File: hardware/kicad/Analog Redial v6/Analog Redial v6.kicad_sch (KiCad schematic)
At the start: 75 parts, among them J1 Barrel_Jack_PTH_Slot, J2 PINHD_1x8_Male, J3 PINHD_1x2_Male, J4 PINHD_1x2_Male, J5 PINHD_2x4_Male, J7 PINHD_1x3_Male, J8 RJ12, J9 RJ12, U1 ESP32-C6-DevKitC-1, U2 ES8388, U3 AG1171, U4 AG1171, U5 XC6206P332MR

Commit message: v6 board: layout and schematic updates, PCBWay production files (Oct 5)
Co-Authored-By: Claude Sonnet 5.5 <noreply@anthropic.com>
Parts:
- C10, C11, C16, C17, D12, H1, H2, H3, H4, J1, J2, J3, J4, J5, J7, J8, J9, U1, U3, U4: now left out of the parts list
- U5: value XC6206P332MR -> XC6206P362MR
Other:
- note added: "Changes for SMD5 - SMD6: need to move passives in ag1171 footprint area for ag1171 real module... touches caps. bigger esp32 holes! they're a little tight 3.6V or 3.7V regulator for bluetooth module (need to check if we should use it for audio chip also?) Do we want to do SMT 470uF caps?"
- note removed: "Changes for SMD6: need to move passives in ag1171 footprint area for ag1171 real module... touches caps. bigger esp32 holes!"
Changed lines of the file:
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@@
 		)
 	)
-	(text "Changes for SMD6:\nneed to move passives in ag1171 footprint area for ag1171 real module...  touches caps.\n\nbigger esp32 holes!\n\n\n"
+	(text "Changes for SMD5 - SMD6:\nneed to move passives in ag1171 footprint area for ag1171 real module...  touches caps.\nbigger esp32 holes!  they're a little tight\n3.6V or 3.7V regulator for bluetooth module (need to check if we should use it for audio chip also?)\nDo we want to do SMT 470uF caps?\n\n\n\n"
 		(exclude_from_sim no)
 		(at 198.628 61.214 0)
@@
 		(body_style 1)
 		(exclude_from_sim no)
-		(in_bom yes)
+		(in_bom no)
 		(on_board yes)
 		(in_pos_files yes)
@@
 		(body_style 1)
 		(exclude_from_sim no)
-		(in_bom yes)
+		(in_bom no)
 		(on_board yes)
 		(in_pos_files yes)
@@
 		(body_style 1)
 		(exclude_from_sim no)
-		(in_bom yes)
+		(in_bom no)
 		(on_board yes)
 		(in_pos_files yes)
@@
 			)
 		)
-		(property "Value" "XC6206P332MR"
+		(property "Value" "XC6206P362MR"
 			(at 101.6 50.8 0)
 			(show_name no)
@@
 		(body_style 1)
 		(exclude_from_sim no)
-		(in_bom yes)
+		(in_bom no)
 		(on_board yes)
 		(in_pos_files yes)
@@
 		(body_style 1)
 		(exclude_from_sim no)
-		(in_bom yes)
+		(in_bom no)
 		(on_board yes)
 		(in_pos_files yes)
@@
 		(body_style 1)
 		(exclude_from_sim no)
-		(in_bom yes)
+		(in_bom no)
 		(on_board yes)
 		(in_pos_files yes)
@@
 		(body_style 1)
 		(exclude_from_sim no)
-		(in_bom yes)
+		(in_bom no)
 		(on_board yes)
 		(in_pos_files yes)
@@
 		(body_style 1)
 		(exclude_from_sim no)
-		(in_bom yes)
+		(in_bom no)
 		(on_board yes)
 		(in_pos_files yes)
@@
 		(body_style 1)
 		(exclude_from_sim no)
-		(in_bom yes)
+		(in_bom no)
 		(on_board yes)
 		(in_pos_files yes)
@@
 		(body_style 1)
 		(exclude_from_sim no)
-		(in_bom yes)
+		(in_bom no)
 		(on_board yes)
 		(in_pos_files yes)
@@
 		(body_style 1)
 		(exclude_from_sim no)
-		(in_bom yes)
+		(in_bom no)
 		(on_board yes)
 		(in_pos_files yes)
@@
 		(body_style 1)
 		(exclude_from_sim no)
-		(in_bom yes)
+		(in_bom no)
 		(on_board yes)
 		(in_pos_files yes)
@@
 		(body_style 1)
 		(exclude_from_sim no)
-		(in_bom yes)
+		(in_bom no)
 		(on_board yes)
 		(in_pos_files yes)
@@
 		(body_style 1)
 		(exclude_from_sim no)
-		(in_bom yes)
+		(in_bom no)
 		(on_board yes)
 		(in_pos_files yes)
@@
 		(body_style 1)
 		(exclude_from_sim no)
-		(in_bom yes)
+		(in_bom no)
 		(on_board yes)
 		(in_pos_files yes)
@@
 		(body_style 1)
 		(exclude_from_sim no)
-		(in_bom yes)
+		(in_bom no)
 		(on_board yes)
 		(in_pos_files yes)
@@
 		(body_style 1)
 		(exclude_from_sim no)
-		(in_bom yes)
+		(in_bom no)
 		(on_board yes)
 		(in_pos_files yes)
@@
 		(body_style 1)
 		(exclude_from_sim no)
-		(in_bom yes)
+		(in_bom no)
 		(on_board yes)
 		(in_pos_files yes)
@@
 		(body_style 1)
 		(exclude_from_sim no)
-		(in_bom yes)
+		(in_bom no)
 		(on_board yes)
 		(in_pos_files yes)
@@
 		(body_style 1)
 		(exclude_from_sim no)
-		(in_bom yes)
+		(in_bom no)
 		(on_board yes)
 		(in_pos_files yes)

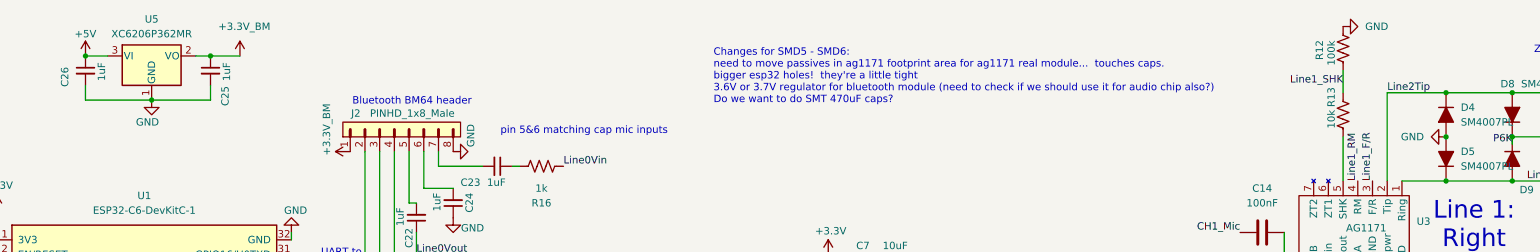
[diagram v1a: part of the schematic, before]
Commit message: v6 board released (untested): clone 5V pin fix, silkscreen updates; JLCPCB export files; docs say untested but should work
U5 stays the 3.3 V XC6206P332MR (JLC Basic); the 3.6 V part was not done.

Co-Authored-By: Claude Sonnet 5.5 <noreply@anthropic.com>
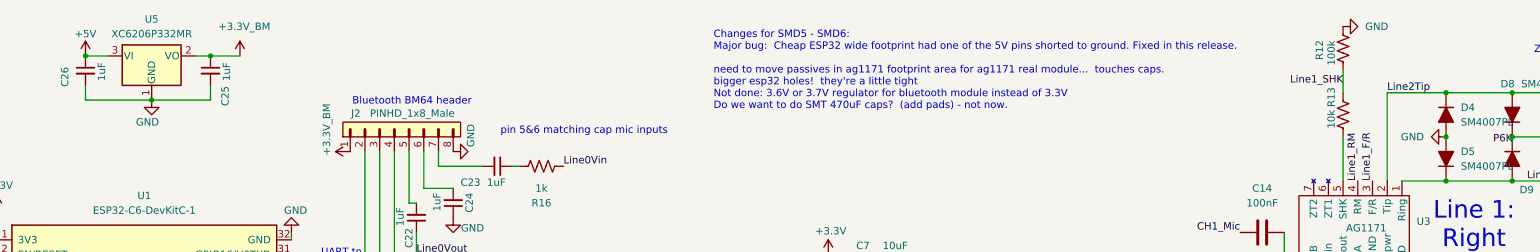
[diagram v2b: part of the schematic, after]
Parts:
- U5: value XC6206P362MR -> XC6206P332MR
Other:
- note added: "Changes for SMD5 - SMD6: Major bug: Cheap ESP32 wide footprint had one of the 5V pins shorted to ground. Fixed in this release. need to move passives in ag1171 footprint area for ag1171 real module... touches caps. bigger esp32 holes! they're a little tight Not done: 3.6V or 3.7V regulator for bluetooth module instead of 3.3V Do we want to do SMT 470uF caps? (add pads) - not now."
- note removed: "Changes for SMD5 - SMD6: need to move passives in ag1171 footprint area for ag1171 real module... touches caps. bigger esp32 holes! they're a little tight 3.6V or 3.7V regulator for bluetooth module (need to check if we should use it for audio chip also?) Do we want to do SMT 470uF caps?"
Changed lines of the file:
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@@
 		)
 	)
-	(text "Changes for SMD5 - SMD6:\nneed to move passives in ag1171 footprint area for ag1171 real module...  touches caps.\nbigger esp32 holes!  they're a little tight\n3.6V or 3.7V regulator for bluetooth module (need to check if we should use it for audio chip also?)\nDo we want to do SMT 470uF caps?\n\n\n\n"
+	(text "Changes for SMD5 - SMD6:\nMajor bug:  Cheap ESP32 wide footprint had one of the 5V pins shorted to ground. Fixed in this release.\n\nneed to move passives in ag1171 footprint area for ag1171 real module...  touches caps.\nbigger esp32 holes!  they're a little tight\nNot done: 3.6V or 3.7V regulator for bluetooth module instead of 3.3V\nDo we want to do SMT 470uF caps?  (add pads) - not now.\n\n\n\n\n"
 		(exclude_from_sim no)
 		(at 198.628 61.214 0)
@@
 			)
 		)
-		(property "Value" "XC6206P362MR"
+		(property "Value" "XC6206P332MR"
 			(at 101.6 50.8 0)
 			(show_name no)

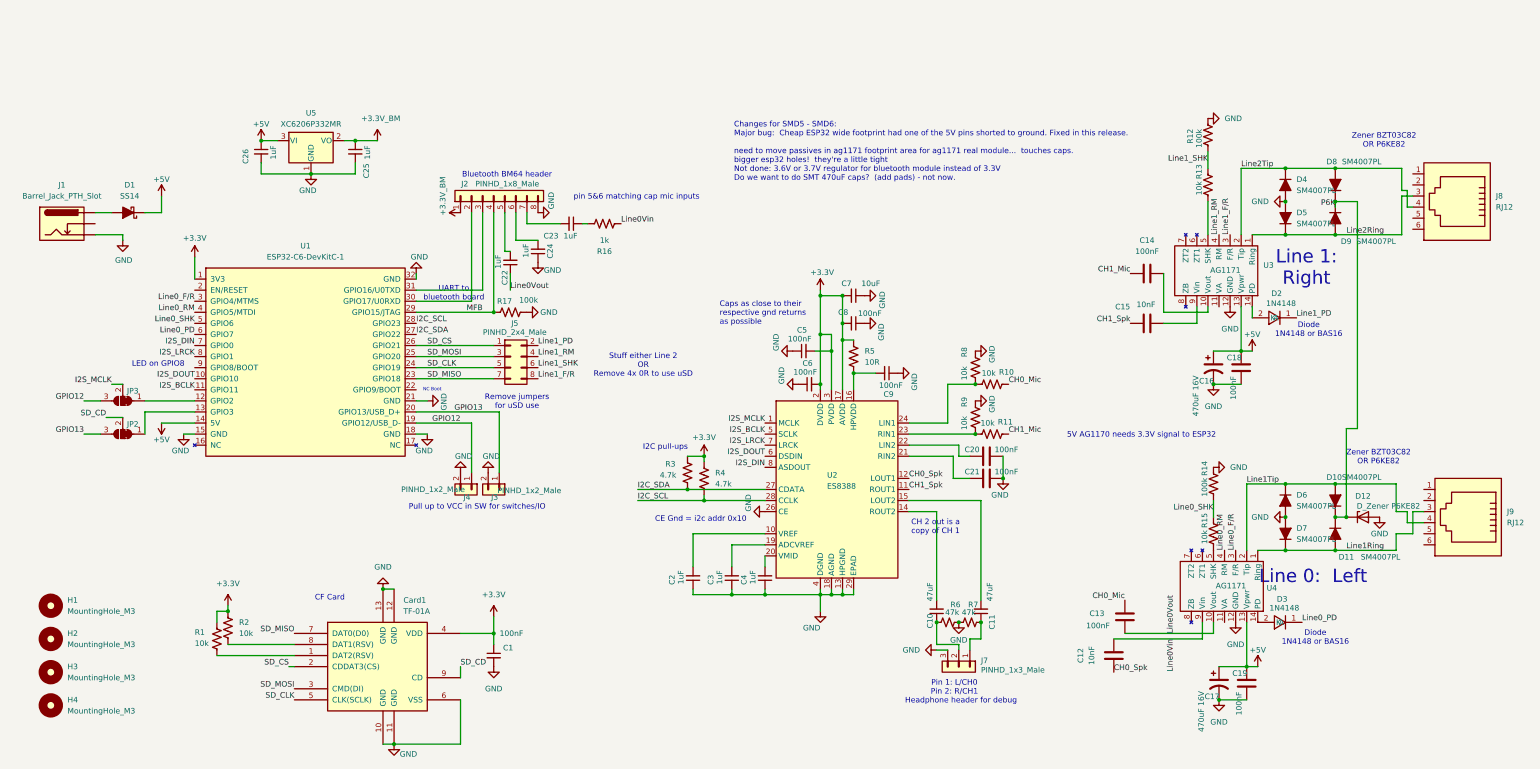
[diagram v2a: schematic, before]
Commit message: v6 KiCad files and exports (SS34 D1, larger power vias, teardrops); PayPhone project and cards; README: fix the v5 board image name (case); ignore KiCad local history and editor backups
Co-Authored-By: Claude Sonnet 5.5 <noreply@anthropic.com>
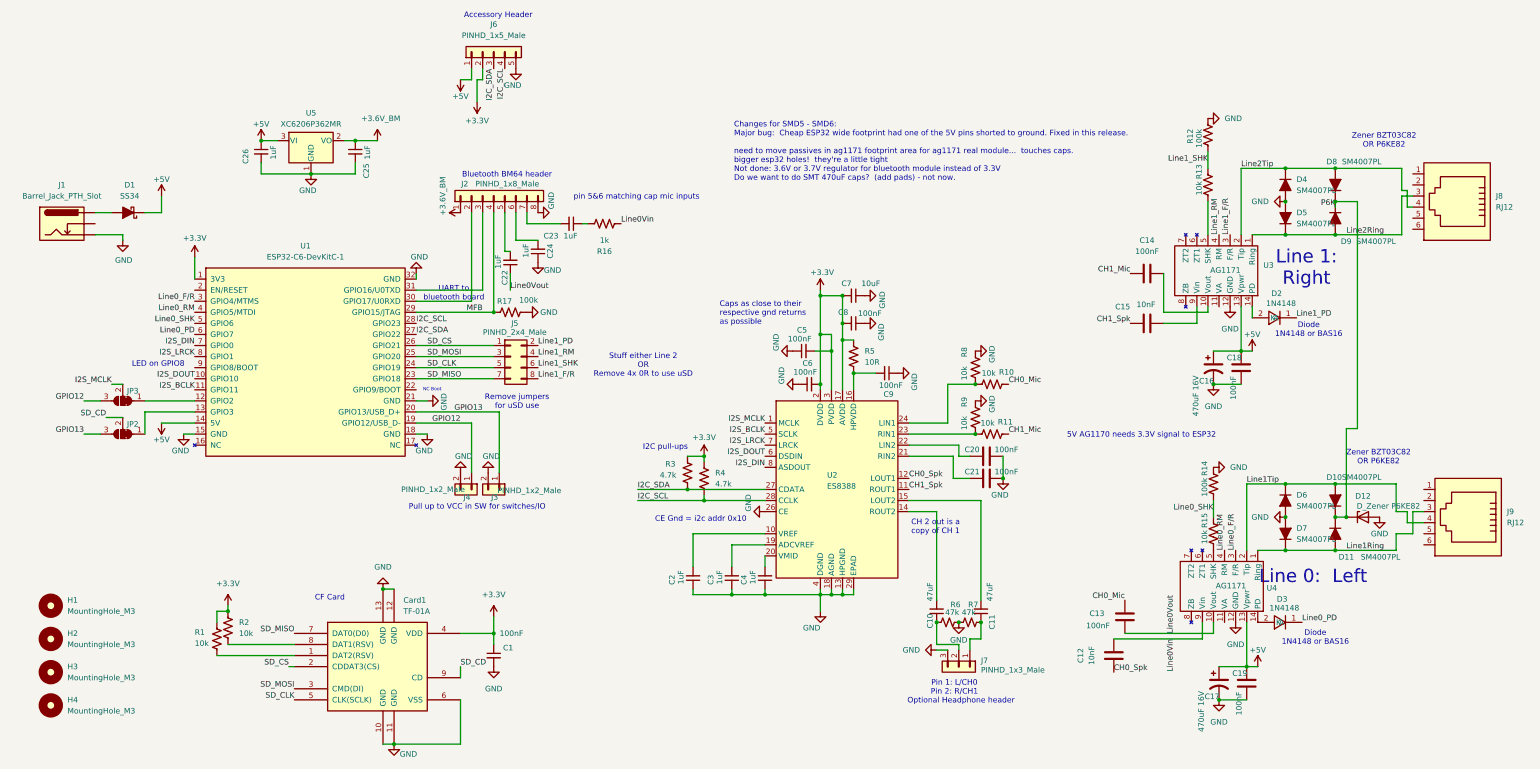
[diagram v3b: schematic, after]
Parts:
- added J6: PINHD_1x5_Male, Connector_PinHeader_2.54mm:PinHeader_1x05_P2.54mm_Vertical, symbol PCM_SL_Pin_Headers:PINHD_1x5_Male
- D1: value SS14 -> SS34
- U5: value XC6206P332MR -> XC6206P362MR
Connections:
- net +3.3V: now also J6.2
- net +5V: now also J6.1
- net GND: now also J6.5
- net I2C_SCL: now also J6.4
- net I2C_SDA: now also J6.3
- net +3.3V_BM renamed +3.6V_BM
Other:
- note added: "Accessory Header"
- note added: "Optional Headphone header"
- note removed: "Headphone header for debug"
